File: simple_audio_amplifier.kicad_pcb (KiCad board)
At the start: 2 copper layers, 80 x 50 mm, 37 parts, among them J1 TB006-508-02BE, J2 PJ-322, J3 TB006-508-02BE, Q1 2N2222A, U1 LM386N-1

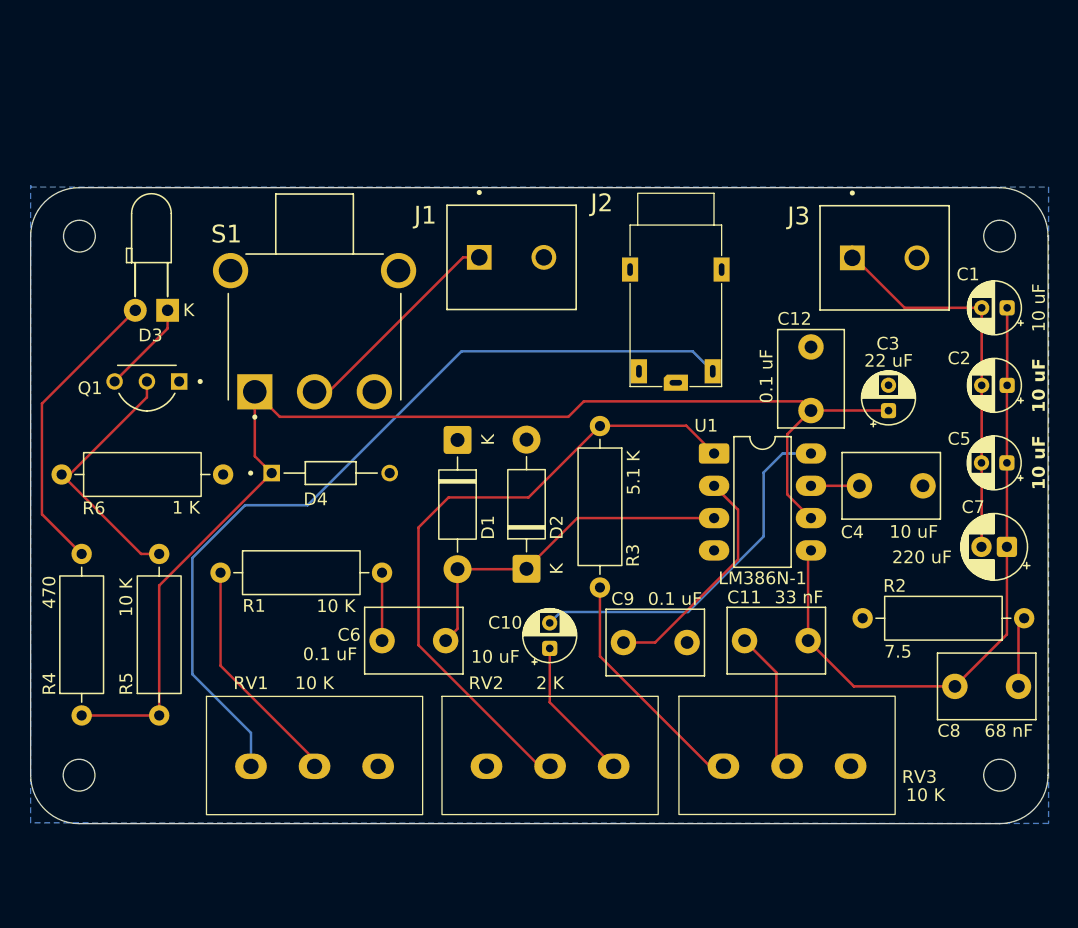
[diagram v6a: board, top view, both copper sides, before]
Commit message: Started PCB design
Fix: fixed some wrong footprints.
Fix: added missing footprint.
Feat: moved the footprints to fit the design.
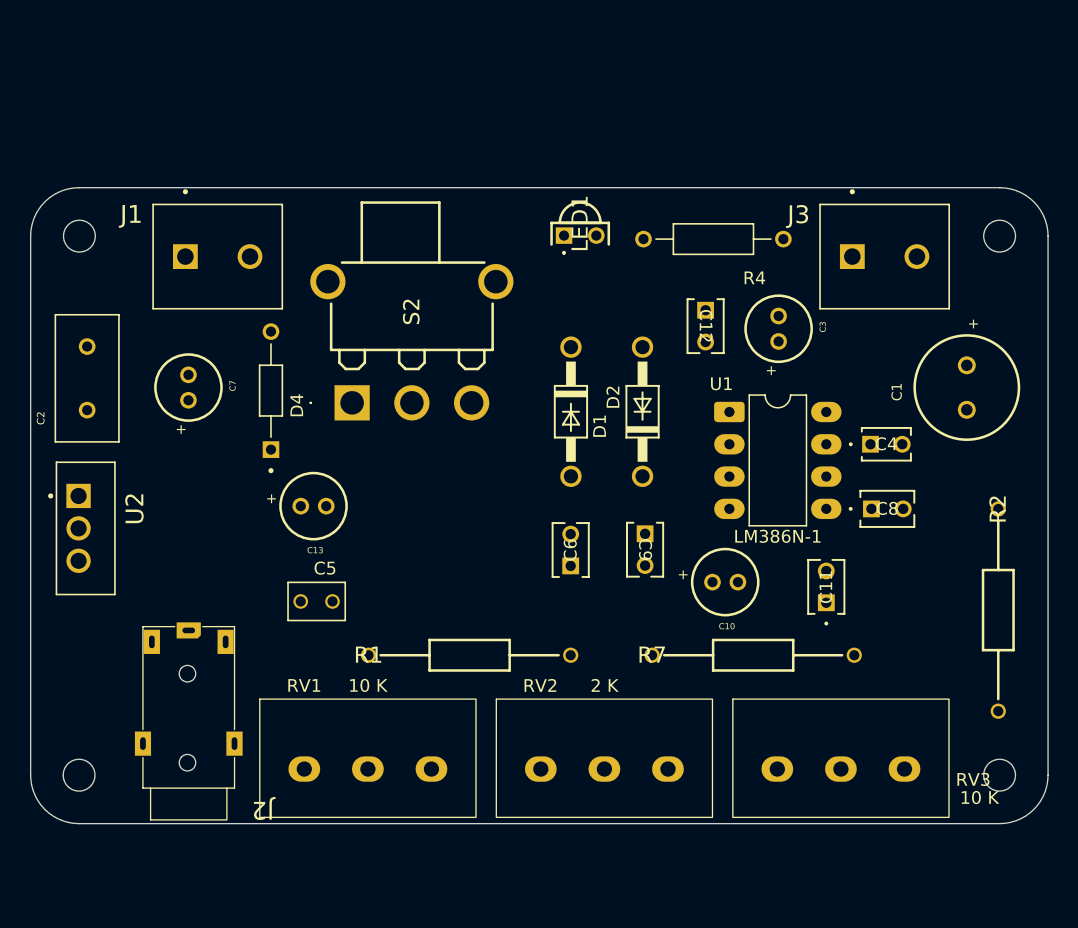
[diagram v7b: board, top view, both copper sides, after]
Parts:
- removed D3: Green LED, LED_THT:LED_D3.0mm_Horizontal_O3.81mm_Z2.0mm
- removed Q1: 2N2222A, 2N2222A:TO92254P470H750-3
- removed R3: 5.1 K, Resistor_THT:R_Axial_DIN0309_L9.0mm_D3.2mm_P12.70mm_Horizontal
- removed R5: 10 K, Resistor_THT:R_Axial_DIN0309_L9.0mm_D3.2mm_P12.70mm_Horizontal
- removed R6: 1 K, Resistor_THT:R_Axial_DIN0309_L9.0mm_D3.2mm_P12.70mm_Horizontal
- removed S1: 500SSP3S1M6QEA, 500SSP3S1M6QEA:SW_500SSP3S1M6QEA
- added C13: 22 uF, WCAP-ATLI_5X11:WCAP-ATLI_5X11_DXL_, F.Cu at (113.0, 95.3)
- added LED1: TLPG5600, TLPG5600:TLPG5600, F.Cu at (132.7, 74.0)
- added R7: 10 K, MF0207FRE52-10K:RESAD1590W60L630D240, F.Cu at (139.7, 107.0)
- added S2: MFP 126 D-RA, MFP126DRA-UL:MFP126DRAUL, F.Cu at (116.1, 87.2)
- added U2: L7805CV, L7805CV:TO255P1040X460X1968-3, F.Cu at (94.5, 94.5)
- C1: value 10 uF -> 270 uF; footprint Capacitor_THT:CP_Radial_D4.0mm_P2.00mm -> 860040574008:WCAP-ATUL_8X20_DXL_
- C10: footprint Capacitor_THT:CP_Radial_D4.0mm_P2.00mm -> WCAP-ATG5_5X11:WCAP-ATG5_5X11_DXL_
- C11: footprint Capacitor_THT:C_Disc_D7.5mm_W5.0mm_P5.00mm -> K333K15X7RF5TL2:CAP_K-SERIES_15-L2_VIS
- C12, C6, C9: footprint Capacitor_THT:C_Disc_D7.5mm_W5.0mm_P5.00mm -> K104K15X7RF5TL2:K104K15X7RF5TL2_VIS
- C2: value 10 uF -> 1 uF; footprint Capacitor_THT:CP_Radial_D4.0mm_P2.00mm -> TAP105K050BRW:XTAL_ZTA-6.00MG
- C3: footprint Capacitor_THT:CP_Radial_D4.0mm_P2.00mm -> WCAP-ATLI_5X11:WCAP-ATLI_5X11_DXL_
- C4: footprint Capacitor_THT:C_Disc_D7.5mm_W5.0mm_P5.00mm -> K103K10X7RF5UL2:K103K10X7RF5UL2_VIS
- C5: value 10 uF -> 2.2 uF; footprint Capacitor_THT:CP_Radial_D4.0mm_P2.00mm -> FG14X7R1H225KRT06:CAPRB250W50L450T300H550
- C7: value 220 uF -> 22 uF; footprint Capacitor_THT:CP_Radial_D5.0mm_P2.00mm -> WCAP-ATLI_5X11:WCAP-ATLI_5X11_DXL_
- C8: footprint Capacitor_THT:C_Disc_D7.5mm_W5.0mm_P5.00mm -> K683K15X7RF5TL2:CAP_K-SERIES_15-L2_VIS
- D1, D2: footprint Diode_THT:D_DO-41_SOD81_P10.16mm_Horizontal -> 1N5819:DO41-10
- D4: value NZX13B,133 -> NZX30C,133
- R1, R2: footprint Resistor_THT:R_Axial_DIN0309_L9.0mm_D3.2mm_P12.70mm_Horizontal -> MF0207FRE52-10K:RESAD1590W60L630D240
- R4: value 470 -> 309; footprint Resistor_THT:R_Axial_DIN0309_L9.0mm_D3.2mm_P12.70mm_Horizontal -> MFR-25FBF52-309R:RESAD1100W55L630D240B
- moved C2 72.3 mm to (95.2, 85.3), turned to 90 degrees
- moved C7 65.6 mm to (103.2, 86.0), turned to -90 degrees
- moved J2 62.5 mm to (95.6, 111.5), turned to 90 degrees
- moved R4 62.2 mm to (144.5, 74.3), turned to 180 degrees
- moved C5 55.4 mm to (113.3, 102.8), turned to 0 degrees
- moved J1 23.1 mm to (103.0, 75.7)
- moved C6 16.0 mm to (133.2, 100.0), turned to 90 degrees
- moved C8 15.4 mm to (156.9, 95.5)
- moved D2 15.4 mm to (138.9, 87.9)
- moved C10 14.8 mm to (145.4, 101.3), turned to 180 degrees
- moved R1 13.3 mm to (117.3, 107.0)
- moved C3 10.8 mm to (149.6, 81.4), turned to -90 degrees
- moved D1 9.19 mm to (133.3, 87.9)
- moved R2 8.83 mm to (166.9, 95.5), turned to -90 degrees
- moved C12 8.77 mm to (143.9, 79.9)
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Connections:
- C1 pad 2: Net-(J3-Pin_1) -> Net-(J3-Pin_2)
- C12 pad 2: +BATT -> +5V0
- C2 pad 1: Net-(C1-Pad1) -> +BATT
- C2 pad 2: Net-(J3-Pin_1) -> GND
- C3 pad 1: +BATT -> +5V0
- C5 pad 1: Net-(C1-Pad1) -> +5V0
- C5 pad 2: Net-(J3-Pin_1) -> GND
- C7 pad 1: Net-(C1-Pad1) -> +BATT
- C7 pad 2: Net-(J3-Pin_1) -> GND
- J3 pad 1: Net-(J3-Pin_1) -> GND
- J3 pad 2: GND -> Net-(J3-Pin_2)
- R4 pad 1: +BATT -> +5V0
- RV1 pad 1: Net-(J2-Pad2) -> GND
- RV1 pad 3: GND -> Net-(J2-Pad2)
- RV2 pad 1: unconnected-(RV2-Pad1) -> Net-(R7-Pad1)
- RV2 pad 2: Net-(R3-Pad1) -> Net-(R7-Pad1)
- RV3 pad 1: Net-(R3-Pad2) -> Net-(C11-Pad1)
- RV3 pad 3: unconnected-(RV3-Pad3) -> Net-(R7-Pad2)
- U1 pad 1: Net-(R3-Pad1) -> Net-(R7-Pad1)
- U1 pad 6: +BATT -> +5V0
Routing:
- net +BATT: track 97.2 -> 0.00 mm
- net Net-(J2-Pad2): track 66.6 -> 0.00 mm
- net Net-(C1-Pad1): track 51.7 -> 0.00 mm
- net Net-(R3-Pad1): track 51.1 -> 0.00 mm
- net Net-(J3-Pin_1): track 31.4 -> 0.00 mm
- net Net-(C10-Pad2): track 29.0 -> 0.00 mm
- net Net-(D1-A): track 27.8 -> 0.00 mm
- net Net-(LED1-A): track 23.5 -> 0.00 mm
- net Net-(Q1-Pad2): track 20.7 -> 0.00 mm
- net Net-(R1-Pad1): track 18.8 -> 0.00 mm
- net Net-(U1--): track 18.3 -> 0.00 mm
- net Net-(R3-Pad2): track 18.0 -> 0.00 mm
- net Net-(J1-Pin_1): track 17.3 -> 0.00 mm
- net Net-(C10-Pad1): track 11.4 -> 0.00 mm
- net Net-(C11-Pad1): track 11.1 -> 0.00 mm
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- removed copper zone on B.Cu, net GND
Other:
- board text removed: "K"

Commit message: Routed the PCB + input mixer
Feat: added PCB tracks (all tracks on one layer).
Perf: added input mixer with new capacitor.
Perf: increased the track width.
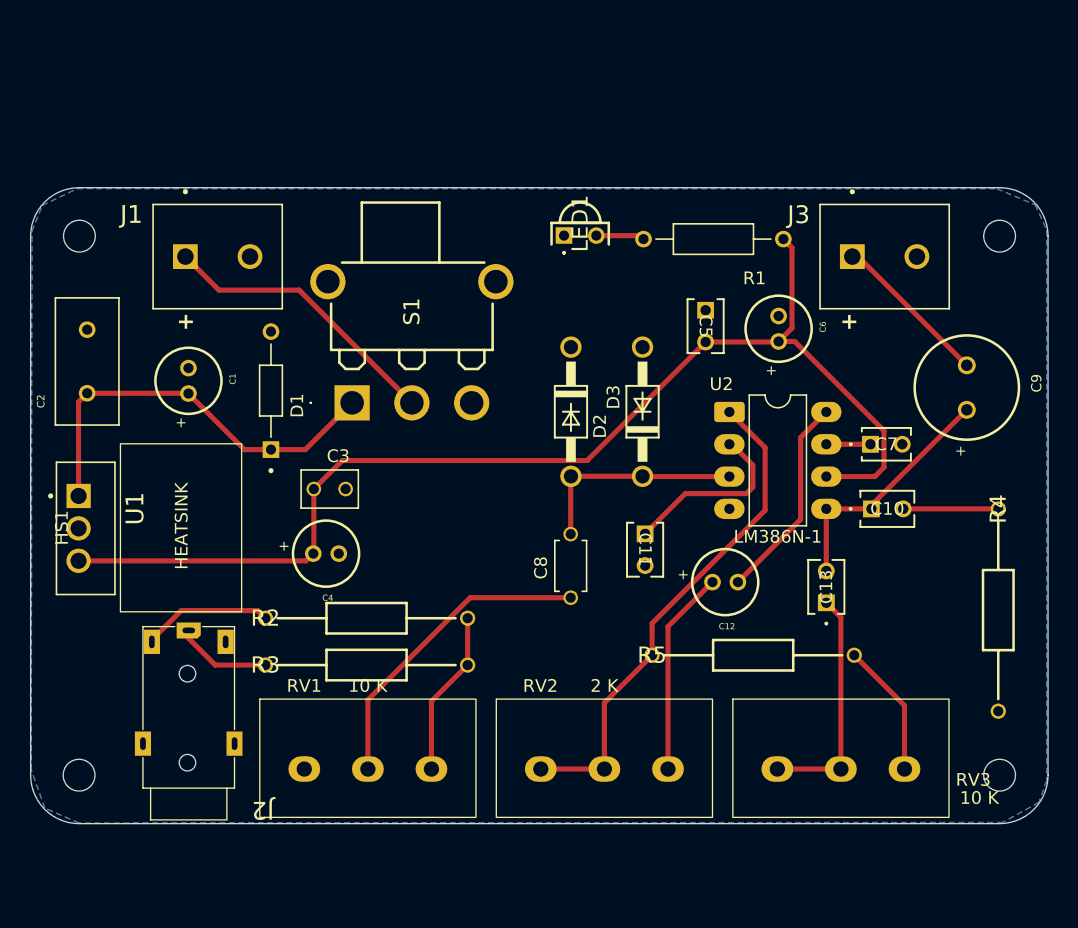
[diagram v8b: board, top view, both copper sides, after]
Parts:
- added HS1: Heatsink, V7236B1:V7236B1, F.Cu at (93.7, 97.0)
- added R3: 1 K, MF0207FTE52-1K:RESAD1590W60L630D240, F.Cu at (109.2, 107.8)
- C8: renamed from C6; value 0.1 uF -> 1 uF; footprint K104K15X7RF5TL2:K104K15X7RF5TL2_VIS -> FG28X5R1H105KRT06:CAPRB500W50L400T250H550
- R2: renamed from R1; value 10 K -> 1 K; footprint MF0207FRE52-10K:RESAD1590W60L630D240 -> MF0207FTE52-1K:RESAD1590W60L630D240
- moved REF** 31.7 mm to (117.4, 111.2)
- moved C3 8.90 mm to (114.3, 94.0)
- moved R2 8.61 mm to (109.2, 104.1)
- moved REF** 7.70 mm to (120.8, 82.4)
- moved C4 3.86 mm to (114.0, 99.1)
- moved C2 1.33 mm to (95.2, 83.9)
- moved C1 0.53 mm to (103.2, 85.5)
- turned C9 to -90 degrees
- renumbered C7 to C1, C8 to C10, C9 to C11, C10 to C12, C11 to C13, C5 to C3, C13 to C4, C12 to C5, C3 to C6, C4 to C7, C1 to C9, D4 to D1, D1 to D2, D2 to D3, R4 to R1, R2 to R4, R7 to R5, S2 to S1, U2 to U1, U1 to U2
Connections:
- C8 pad 1: Net-(C6-Pad1) -> Net-(C8-Pad1)
- C9 pad 2: Net-(J3-Pin_2) -> Net-(J3-Pin_1)
- J2 pad 1: unconnected-(J2-Pad1) -> Net-(J2-Pad1)
- J3 pad 1: GND -> Net-(J3-Pin_1)
- J3 pad 2: Net-(J3-Pin_2) -> GND
- R2 pad 1: Net-(R1-Pad1) -> Net-(J2-Pad2)
- R2 pad 2: Net-(C6-Pad1) -> Net-(R2-Pad2)
- RV1 pad 2: Net-(R1-Pad1) -> Net-(C8-Pad1)
- RV1 pad 3: Net-(J2-Pad2) -> Net-(R2-Pad2)
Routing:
- net +5V0: track 0.00 -> 92.9 mm
- net Net-(R5-Pad1): track 0.00 -> 39.5 mm
- net +BATT: track 0.00 -> 32.6 mm
- net Net-(C8-Pad1): track 0.00 -> 24.7 mm
- net Net-(J1-Pin_1): track 0.00 -> 22.6 mm
- net Net-(C10-Pad1): track 0.00 -> 19.3 mm
- net Net-(C13-Pad1): track 0.00 -> 18.6 mm
- net Net-(D2-A): track 0.00 -> 17.0 mm
- net Net-(C12-Pad2): track 0.00 -> 16.3 mm
- net Net-(C12-Pad1): track 0.00 -> 16.1 mm
- net Net-(U2--): track 0.00 -> 14.2 mm
- net Net-(R2-Pad2): track 0.00 -> 13.0 mm
- net Net-(J3-Pin_1): track 0.00 -> 12.5 mm
- net Net-(R5-Pad2): track 0.00 -> 10.6 mm
- net Net-(J2-Pad2): track 0.00 -> 10.3 mm
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- added copper zone on B.Cu, net GND
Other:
- board text added: "+"
- board text added: "Designed by: Circuitry Passion"
- board text added: "Version: 2.0"
- board text removed: "Designed by: F.G."
- board text removed: "Version: 1.0"
